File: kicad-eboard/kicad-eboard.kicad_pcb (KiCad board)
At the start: 4 copper layers, 67.2 x 90 mm, 97 parts, among them J1 Conn_02x03, J2 Conn_01x02, J3 Conn_01x10, M1 Hopper_Servo, SW1 LIMIT_1, SW2 LIMIT_2, SW3 SRX_Encoder, U1 TinkerBoard, U10 REF2033, U11 PDQ15-Q24-S12-D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

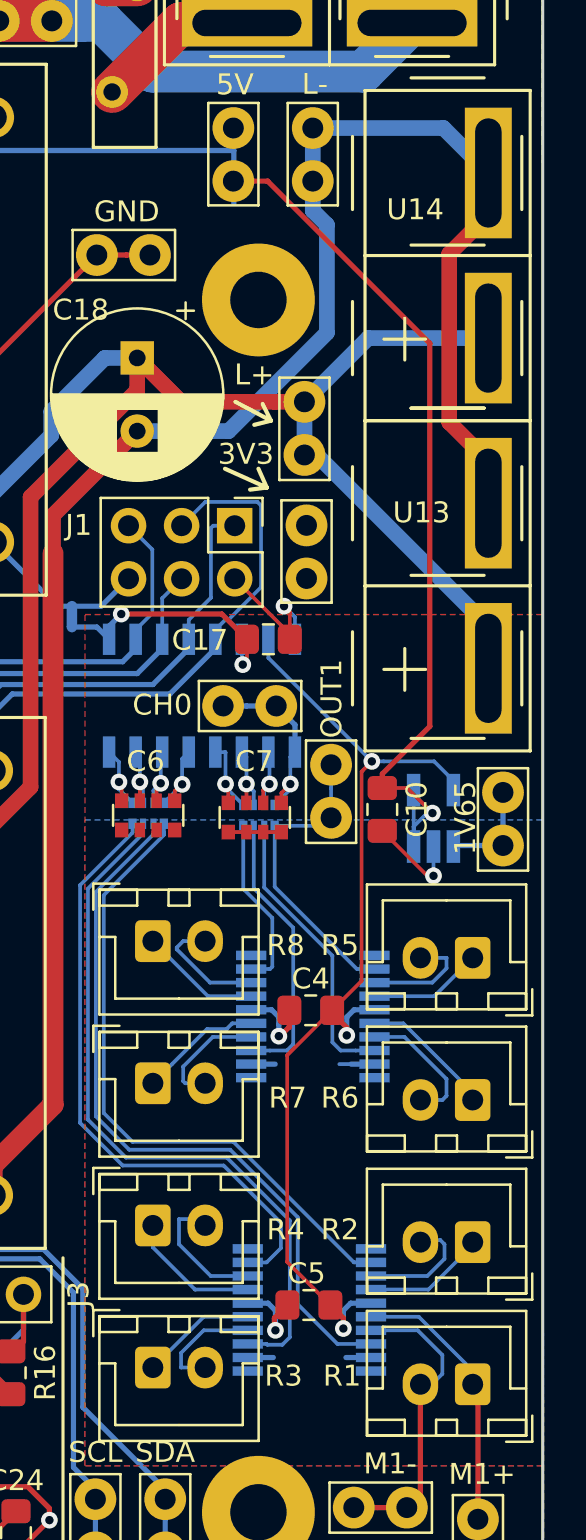
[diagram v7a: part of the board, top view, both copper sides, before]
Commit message: Fix some unconnected nets
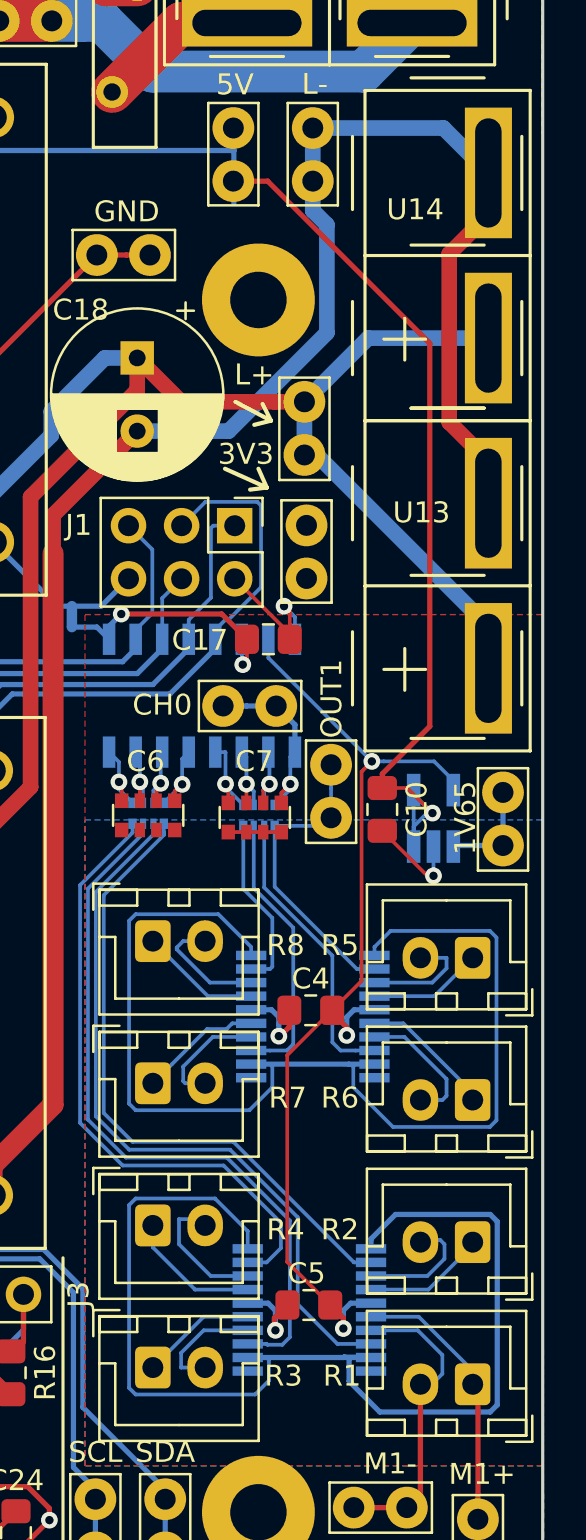
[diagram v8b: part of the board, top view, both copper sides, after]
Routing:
- net +1.65V: track 10.2 -> 118.9 mm
- net +5V: track 200.9 -> 202.0 mm
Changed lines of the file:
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@@
-(kicad_pcb (version 20171130) (host pcbnew 5.0.2+dfsg1-1)
+(kicad_pcb (version 20171130) (host pcbnew "(5.1.5)-3")
   (general
     (thickness 1.6)
     (drawings 24)
-    (tracks 877)
+    (tracks 927)
     (zones 0)
     (modules 97)
@@
     (zone_45_only no)
     (trace_min 0.1778)
-    (segment_width 0.2)
-    (edge_width 0.15)
     (via_size 0.8)
     (via_drill 0.4)
@@
     (uvia_min_size 0.2)
     (uvia_min_drill 0.1)
+    (edge_width 0.15)
+    (segment_width 0.2)
     (pcb_text_width 0.3)
     (pcb_text_size 1.5 1.5)
@@
     (visible_elements 7FFFFF7F)
     (pcbplotparams
-      (layerselection 0x000e0_ffffffff)
+      (layerselection 0x010f0_fffffff9)
       (usegerberextensions true)
       (usegerberattributes false)
@@
       (drillshape 0)
       (scaleselection 1)
-      (outputdirectory "20191229test/"))
+      (outputdirectory "./20200224/"))
   )
   (net 0 "")
@@
   (segment (start 76.2 31.24) (end 77.84 31.24) (width 0.25) (layer F.Cu) (net 7))
   (segment (start 77.84 31.24) (end 85.6 39) (width 0.25) (layer F.Cu) (net 7))
+  (segment (start 76.225 28.725) (end 76.2 28.7) (width 0.25) (layer B.Cu) (net 7))
+  (segment (start 76.225 29.775) (end 76.225 28.725) (width 0.25) (layer B.Cu) (net 7))
   (segment (start 64.345 86.25) (end 64.345 87.92) (width 0.25) (layer F.Cu) (net 8))
   (via (at 64.345 86.25) (size 0.8) (drill 0.4) (layers F.Cu B.Cu) (net 8))
@@
   (segment (start 58.94958 81.049979) (end 60.249601 82.35) (width 0.25) (layer B.Cu) (net 11))
   (segment (start 82.951252 73.483446) (end 81.826252 73.483446) (width 0.25) (layer B.Cu) (net 12))
-  (segment (start 82.787232 87.520053) (end 81.589645 87.520053) (width 0.25) (layer B.Cu) (net 12))
-  (segment (start 77.051252 73.483446) (end 78.201252 73.483446) (width 0.25) (layer B.Cu) (net 12))
-  (segment (start 76.887232 87.520053) (end 78.112859 87.520053) (width 0.25) (layer B.Cu) (net 12))
-  (segment (start 81.826252 73.483446) (end 81.266554 73.483446) (width 0.1778) (layer B.Cu) (net 12))
   (segment (start 86.775 63.025) (end 86.725 63.075) (width 0.25) (layer B.Cu) (net 12))
   (segment (start 89.1 63.025) (end 86.775 63.025) (width 0.25) (layer B.Cu) (net 12))
   (segment (start 89.1 63.025) (end 89.1 60.485) (width 0.25) (layer B.Cu) (net 12))
+  (segment (start 81.733446 73.483446) (end 81.75 73.5) (width 0.25) (layer B.Cu) (net 12))
+  (segment (start 77.051252 73.483446) (end 81.733446 73.483446) (width 0.25) (layer B.Cu) (net 12))
+  (segment (start 81.826252 73.483446) (end 81.75 73.5) (width 0.1778) (layer B.Cu) (net 12))
+  (segment (start 81.75 73.5) (end 81.266554 73.483446) (width 0.1778) (layer B.Cu) (net 12))
+  (segment (start 81.479947 87.520053) (end 81.5 87.5) (width 0.25) (layer B.Cu) (net 12))
+  (segment (start 76.887232 87.520053) (end 81.479947 87.520053) (width 0.25) (layer B.Cu) (net 12))
+  (segment (start 82.787232 87.520053) (end 81.5 87.5) (width 0.25) (layer B.Cu) (net 12))
+  (segment (start 81.5 87.5) (end 81.589645 87.520053) (width 0.25) (layer B.Cu) (net 12))
+  (segment (start 81.937351 73.594547) (end 82.048452 73.483446) (width 0.1778) (layer B.Cu) (net 12))
+  (segment (start 83.836694 76.48891) (end 81.937351 74.589567) (width 0.1778) (layer B.Cu) (net 12))
+  (segment (start 82.048452 73.483446) (end 82.951252 73.483446) (width 0.1778) (layer B.Cu) (net 12))
+  (segment (start 88.473226 76.48891) (end 83.836694 76.48891) (width 0.1778) (layer B.Cu) (net 12))
+  (segment (start 88.78891 76.173226) (end 88.473226 76.48891) (width 0.1778) (layer B.Cu) (net 12))
+  (segment (start 81.937351 74.589567) (end 81.937351 73.594547) (width 0.1778) (layer B.Cu) (net 12))
+  (segment (start 88.473226 67.11109) (end 88.78891 67.426774) (width 0.1778) (layer B.Cu) (net 12))
+  (segment (start 88.78891 67.426774) (end 88.78891 76.173226) (width 0.1778) (layer B.Cu) (net 12))
+  (segment (start 83.720808 67.11109) (end 88.473226 67.11109) (width 0.1778) (layer B.Cu) (net 12))
+  (segment (start 82.951252 67.880646) (end 83.720808 67.11109) (width 0.1778) (layer B.Cu) (net 12))
+  (segment (start 82.951252 68.283446) (end 82.951252 67.880646) (width 0.1778) (layer B.Cu) (net 12))
+  (segment (start 77.901133 87.631154) (end 77.790032 87.520053) (width 0.1778) (layer B.Cu) (net 12))
+  (segment (start 77.901133 88.626174) (end 77.901133 87.631154) (width 0.1778) (layer B.Cu) (net 12))
+  (segment (start 77.790032 87.520053) (end 76.887232 87.520053) (width 0.1778) (layer B.Cu) (net 12))
+  (segment (start 71.21109 88.973226) (end 71.526774 89.28891) (width 0.1778) (layer B.Cu) (net 12))
+  (segment (start 71.21109 80.226774) (end 71.21109 88.973226) (width 0.1778) (layer B.Cu) (net 12))
+  (segment (start 71.526774 79.91109) (end 71.21109 80.226774) (width 0.1778) (layer B.Cu) (net 12))
+  (segment (start 77.238397 89.28891) (end 77.901133 88.626174) (width 0.1778) (layer B.Cu) (net 12))
+  (segment (start 71.526774 89.28891) (end 77.238397 89.28891) (width 0.1778) (layer B.Cu) (net 12))
+  (segment (start 75.321751 79.91109) (end 71.526774 79.91109) (width 0.1778) (layer B.Cu) (net 12))
+  (segment (start 76.887232 81.476571) (end 75.321751 79.91109) (width 0.1778) (layer B.Cu) (net 12))
+  (segment (start 76.887232 82.320053) (end 76.887232 81.476571) (width 0.1778) (layer B.Cu) (net 12))
+  (segment (start 82.787232 81.845053) (end 82.787232 82.320053) (width 0.25) (layer B.Cu) (net 12))
+  (segment (start 83.957295 80.67499) (end 82.787232 81.845053) (width 0.25) (layer B.Cu) (net 12))
+  (segment (start 88.82501 81.01182) (end 88.48818 80.67499) (width 0.25) (layer B.Cu) (net 12))
+  (segment (start 88.82501 89.78818) (end 88.82501 81.01182) (width 0.25) (layer B.Cu) (net 12))
+  (segment (start 88.48818 80.67499) (end 83.957295 80.67499) (width 0.25) (layer B.Cu) (net 12))
+  (segment (start 83.207187 90.12501) (end 88.48818 90.12501) (width 0.25) (layer B.Cu) (net 12))
+  (segment (start 88.48818 90.12501) (end 88.82501 89.78818) (width 0.25) (layer B.Cu) (net 12))
+  (segment (start 81.737231 88.655054) (end 83.207187 90.12501) (width 0.25) (layer B.Cu) (net 12))
+  (segment (start 81.737231 87.595054) (end 81.737231 88.655054) (width 0.25) (layer B.Cu) (net 12))
+  (segment (start 81.812232 87.520053) (end 81.737231 87.595054) (width 0.25) (layer B.Cu) (net 12))
+  (segment (start 82.787232 87.520053) (end 81.812232 87.520053) (width 0.25) (layer B.Cu) (net 12))
+  (segment (start 71.526774 66.31109) (end 71.21109 66.626774) (width 0.1778) (layer B.Cu) (net 12))
+  (segment (start 77.051252 67.880646) (end 75.481696 66.31109) (width 0.1778) (layer B.Cu) (net 12))
+  (segment (start 75.481696 66.31109) (end 71.526774 66.31109) (width 0.1778) (layer B.Cu) (net 12))
+  (segment (start 76.96581 75.68891) (end 78.065153 74.589567) (width 0.1778) (layer B.Cu) (net 12))
+  (segment (start 77.051252 68.283446) (end 77.051252 67.880646) (width 0.1778) (layer B.Cu) (net 12))
+  (segment (start 71.21109 66.626774) (end 71.21109 75.373226) (width 0.1778) (layer B.Cu) (net 12))
+  (segment (start 71.21109 75.373226) (end 71.526774 75.68891) (width 0.1778) (layer B.Cu) (net 12))
+  (segment (start 71.526774 75.68891) (end 76.96581 75.68891) (width 0.1778) (layer B.Cu) (net 12))
+  (segment (start 78.065153 74.589567) (end 78.065153 73.594547) (width 0.1778) (layer B.Cu) (net 12))
+  (segment (start 78.065153 73.594547) (end 77.954052 73.483446) (width 0.1778) (layer B.Cu) (net 12))
+  (segment (start 77.954052 73.483446) (end 77.051252 73.483446) (width 0.1778) (layer B.Cu) (net 12))
   (segment (start 87.9 89.05) (end 87.65 88.8) (width 0.25) (layer F.Cu) (net 13))
   (segment (start 87.9 95.26) (end 87.9 89.05) (width 0.25) (layer F.Cu) (net 13))
